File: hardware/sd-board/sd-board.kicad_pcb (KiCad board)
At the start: 2 copper layers, 25.4 x 78.2 mm, 23 parts, among them J1 TF-01A push-push, J2 FPC 10P 0.5mm (IN), J3 FPC 10P 0.5mm top contact (LC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, U1 74LVC1G04, U2 USBLC6-2SC6, U3 USBLC6-2SC6

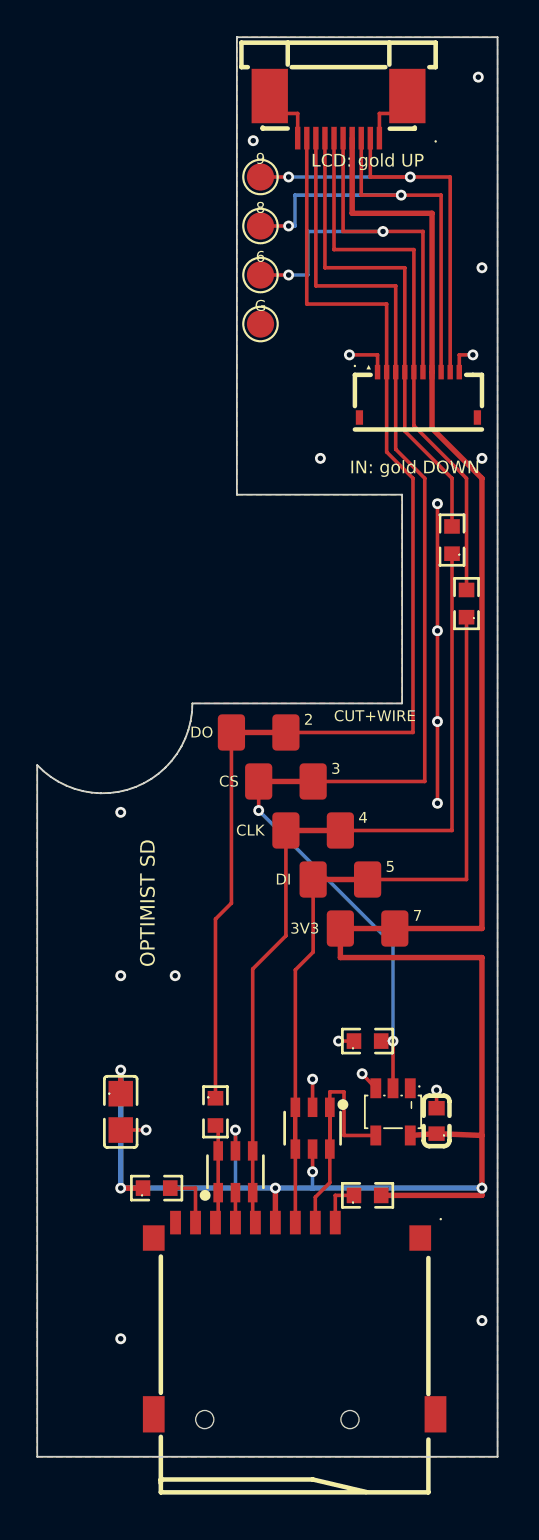
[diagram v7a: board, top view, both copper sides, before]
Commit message: fix(sd-board): Julius's prototype review: R1 220 Ohm (C22962: a card left in SPI mode against D/C, 15 mA not 33), R5/R6 510 Ohm (C23193: the stock screen blank with a native-mode card at CLK direct, fine at 510), R7 47k DAT0 pull-up, FB1 ferrite (C1002) from JP5 to the card's supply and C3 100 nF on its VDD line, TP5 on the socket's DET; DRC 0, nets 82 = 82, mockups regenerated (0 open edges); README: must-pass cold-boot bench test with stock and SLOOP, hot insertion, J3's numbering check; SD-CARD-DESIGN: the prototype's measurements, the R1 timing trade
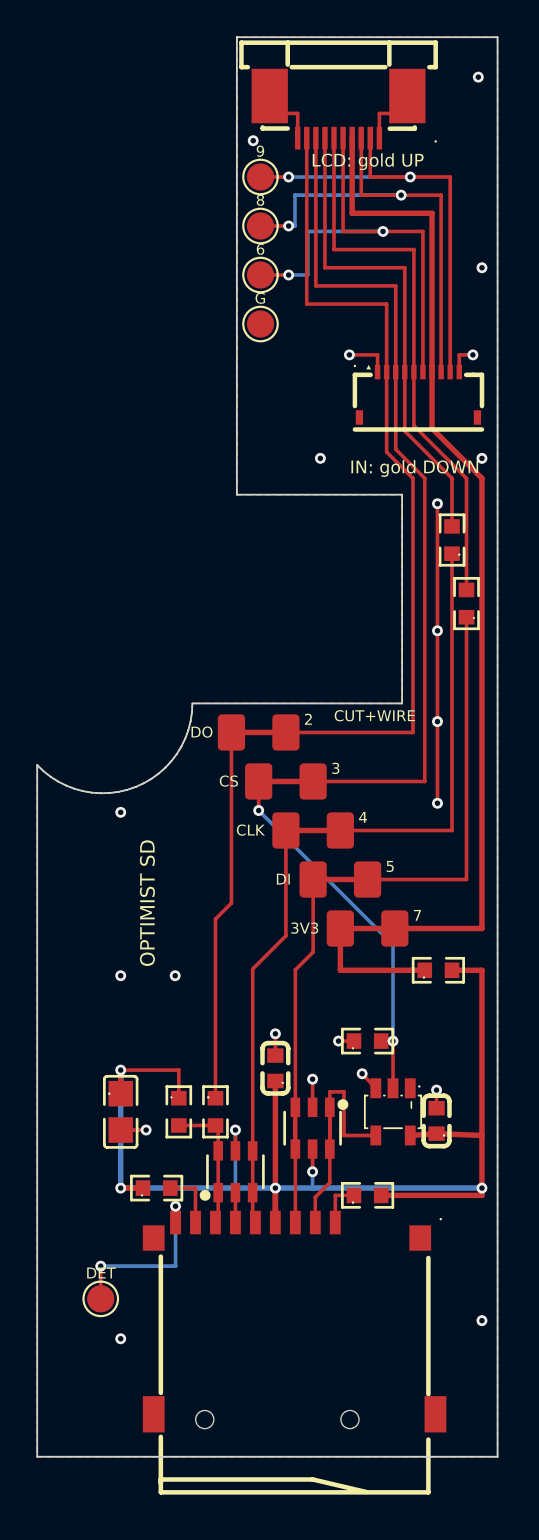
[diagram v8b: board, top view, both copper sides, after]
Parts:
- added C3: 100nF, sdboard:C0603, F.Cu at (184.5, 180.1)
- added FB1: 600R@100MHz, sdboard:R0603, F.Cu at (193.5, 174.7)
- added R7: 47k, sdboard:R0603, F.Cu at (179.2, 182.5)
- added TP5: J12 DET, TestPoint:TestPoint_Pad_D1.5mm, F.Cu at (174.9, 192.8)
- R1: value 100 -> 220
- R5, R6: value 100 -> 510
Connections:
- J1 pad 9: (no net) -> CARD_DET
- JP5 pad 1: SD_VDD -> SD_VIN
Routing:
- net CARD_DET: track 0.00 -> 10.1 mm, vias 0 -> 2
- net SD_VIN: track 0.00 -> 6.95 mm
- net SD_VDD: track 69.3 -> 73.4 mm
- net DAT0: track 5.50 -> 7.52 mm
- net GND: track 34.0 -> 35.2 mm, vias 21 -> 22
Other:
- board text added: "DET"
